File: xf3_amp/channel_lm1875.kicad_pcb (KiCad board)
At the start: 2 copper layers, 76 x 50 mm, 27 parts, among them P1 xhole, P2 CONN_01X03, P3 CONN_01X02, P4 CONN_01X03, P5 INPUT, P6 xhole, P7 xhole, P8 xhole, U1 LM1875

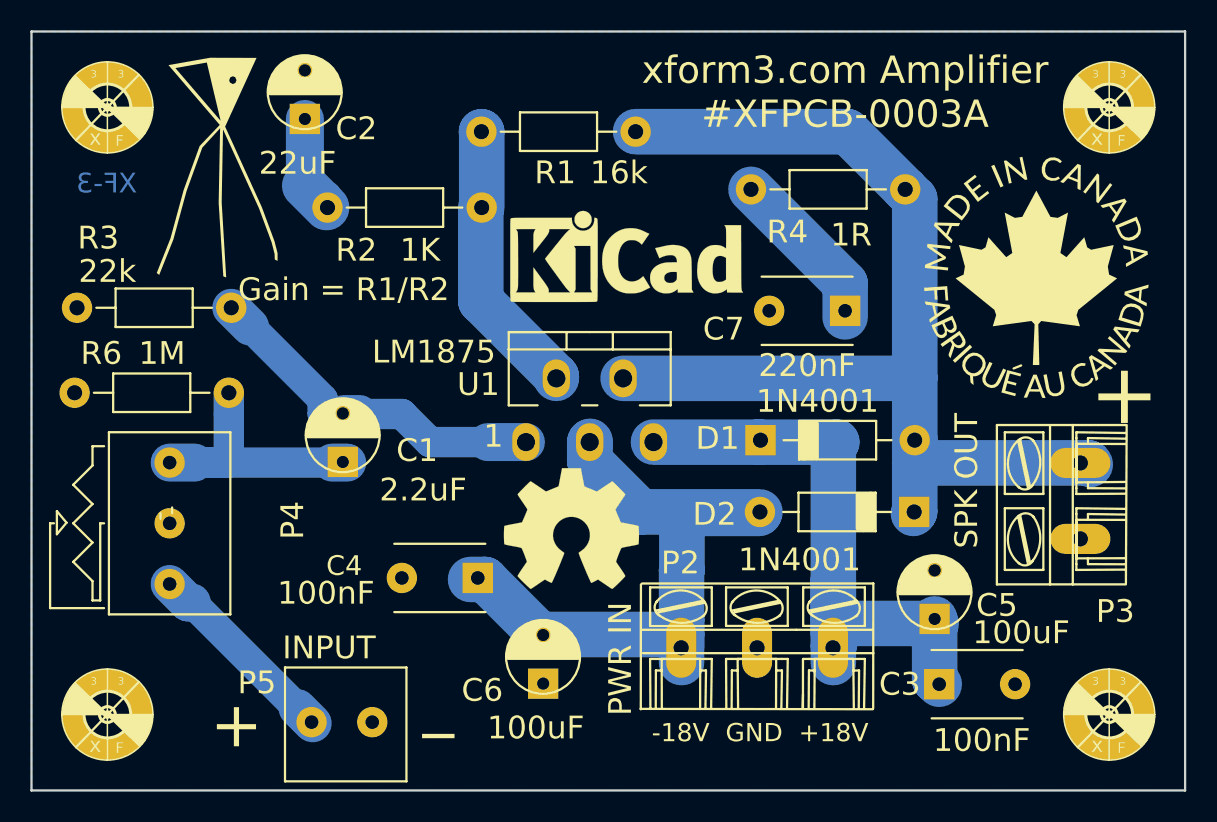
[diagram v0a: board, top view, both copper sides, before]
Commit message: added pictures, updated pcb, silk
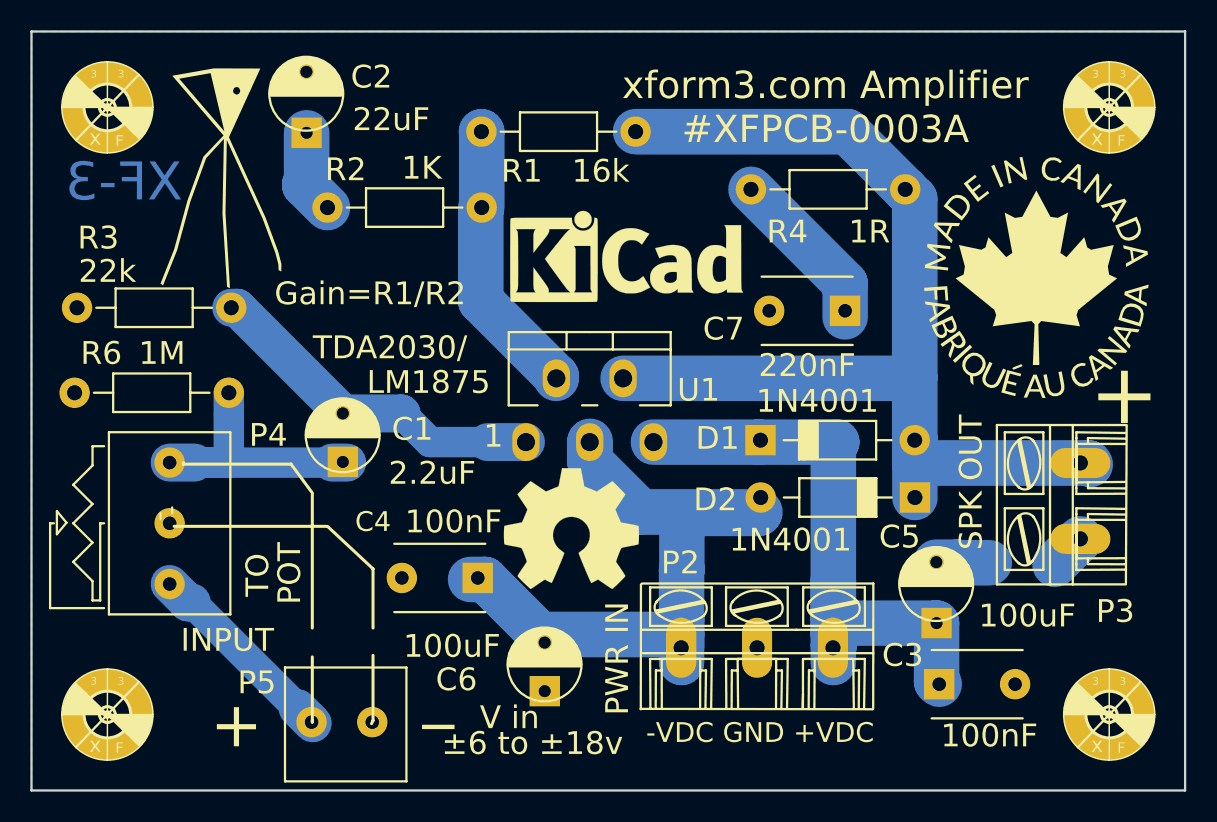
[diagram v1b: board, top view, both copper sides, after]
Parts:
- C2, C5: footprint xlib:x_Cap_Radial_7mm -> x_components:x_CapRadial7mm
- moved D2 0.95 mm to (58.2, 30.7)
- moved svg2mod 0.74 mm to (11.6, 9.40)
- moved C5 0.55 mm to (59.6, 37.4)
- moved C6 0.51 mm to (33.8, 42.7)
- moved C2 0.14 mm to (18.1, 5.10)
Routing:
- net GND: track 0.00 -> 5.88 mm
- net Net-(C2-Pad1): track 7.20 -> 5.75 mm
- net Net-(C1-Pad2): track 23.7 -> 23.1 mm
- net /OUT: track 71.9 -> 72.4 mm
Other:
- board text added: "-VDC GND +VDC"
- board text added: "Gain=R1/R2"
- board text added: "POT"
- board text added: "TDA2030/"
- board text added: "TO"
- board text added: "V in"
- board text added: "±6 to ±18v"
- board text removed: "-18V GND +18V"
- board text removed: "Gain = R1/R2"
